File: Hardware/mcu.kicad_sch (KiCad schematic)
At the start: 20 parts, among them J2 Conn_01x03, SW2 SW_Push, SW3 SW_Push, U2 W25Q128JVS, U3 RP2040, Y1 ABM8-272-T3

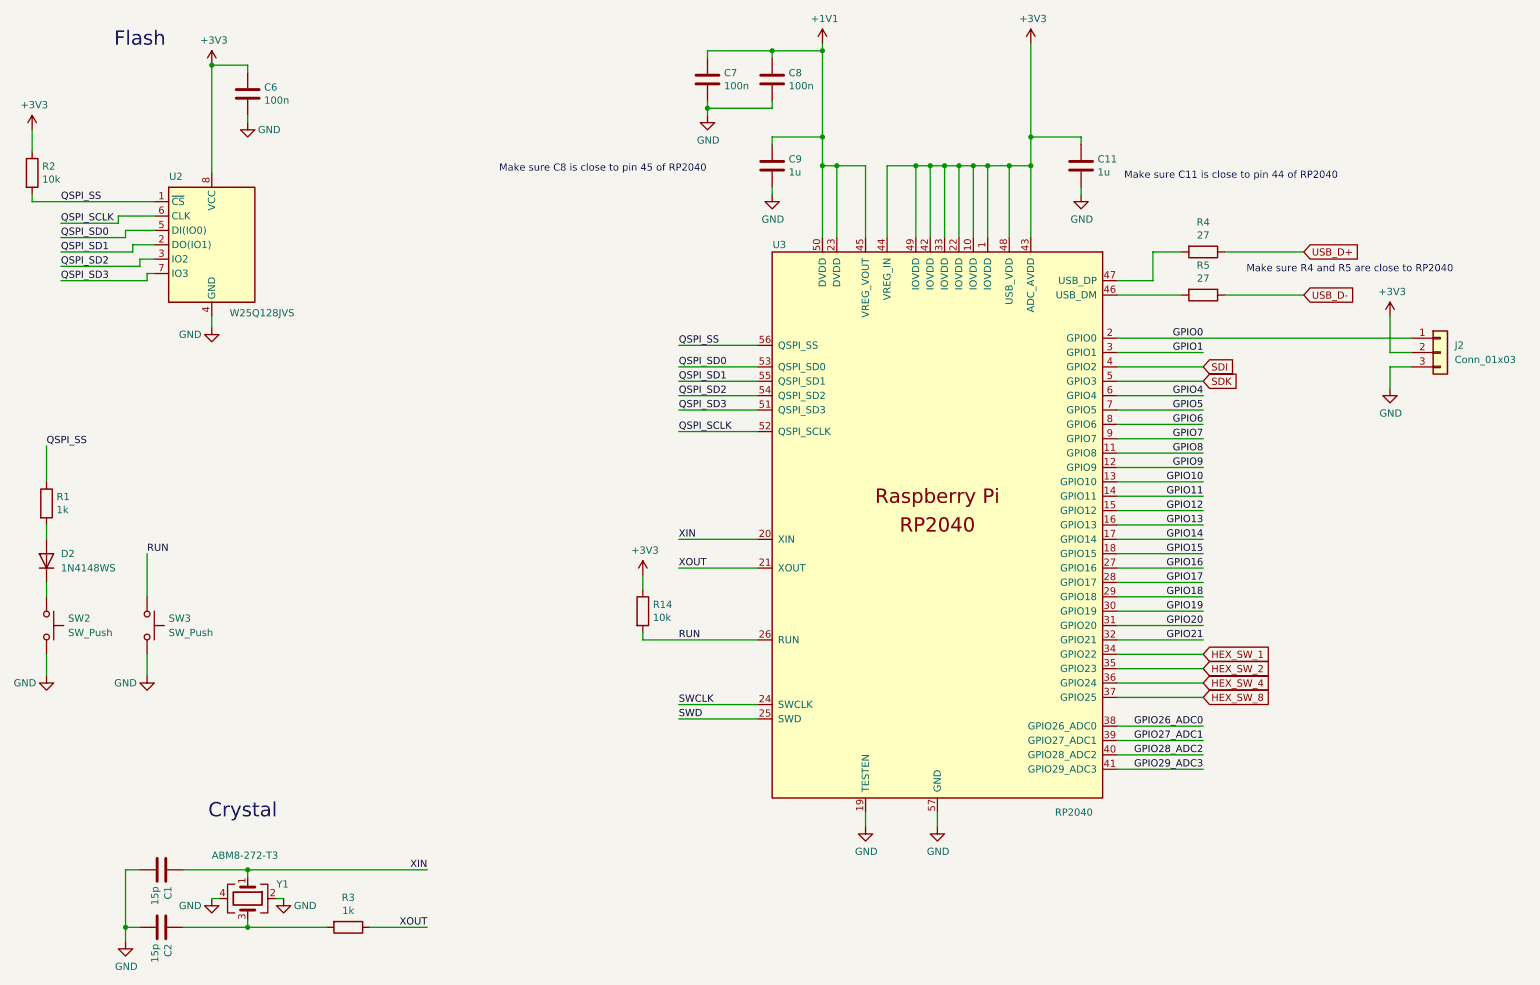
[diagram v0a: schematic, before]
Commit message: Added new components to sch and pcb and redid the routing and layout of pcb
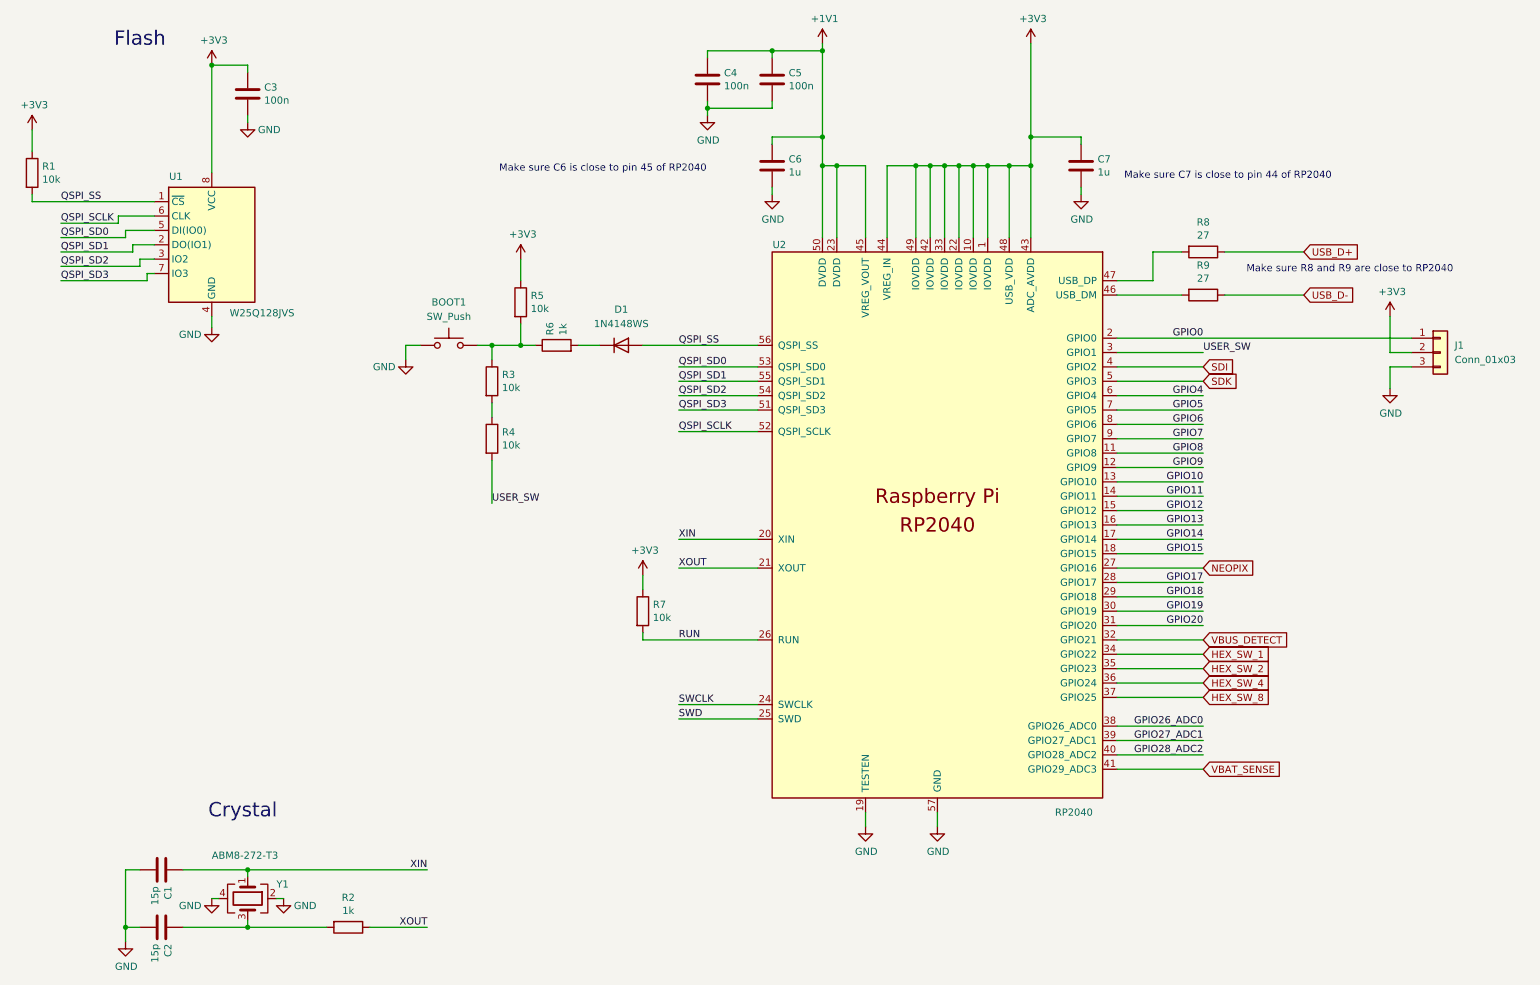
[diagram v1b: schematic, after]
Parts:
- removed SW3: SW_Push, duso:NanoT-AS, symbol Switch:SW_Push
- added R3, R4, R5: 10k, Resistor_SMD:R_0402_1005Metric, symbol Device:R
- renumbered SW2 to BOOT1, C6 to C3, C7 to C4, C8 to C5, C9 to C6, C11 to C7, D2 to D1, J2 to J1, R2 to R1, R3 to R2, R1 to R6, R14 to R7, R4 to R8, R5 to R9, U2 to U1, U3 to U2
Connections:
- net +3V3: now also R5.1
- net GND: now also BOOT1.1; no longer BOOT1.2
- net QSPI_SS: now also D1.2 (A); no longer R6.1
- net at D1.1 (K): now also R6.2; no longer BOOT1.1
- net GPIO1 renamed USER_SW
- net USER_SW: now also R4.2
- net GPIO16 renamed NEOPIX
- net GPIO21 renamed VBUS_DETECT
- net GPIO29_ADC3 renamed VBAT_SENSE
- new net: R3.2, R4.1
- new net: BOOT1.2, R3.1, R5.2, R6.1
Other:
- note added: "Make sure C6 is close to pin 45 of RP2040"
- note added: "Make sure C7 is close to pin 44 of RP2040"
- note added: "Make sure R8 and R9 are close to RP2040"
- note removed: "Make sure C11 is close to pin 44 of RP2040"
- note removed: "Make sure C8 is close to pin 45 of RP2040"
- note removed: "Make sure R4 and R5 are close to RP2040"
- moved on the sheet: BOOT1, D1, R6

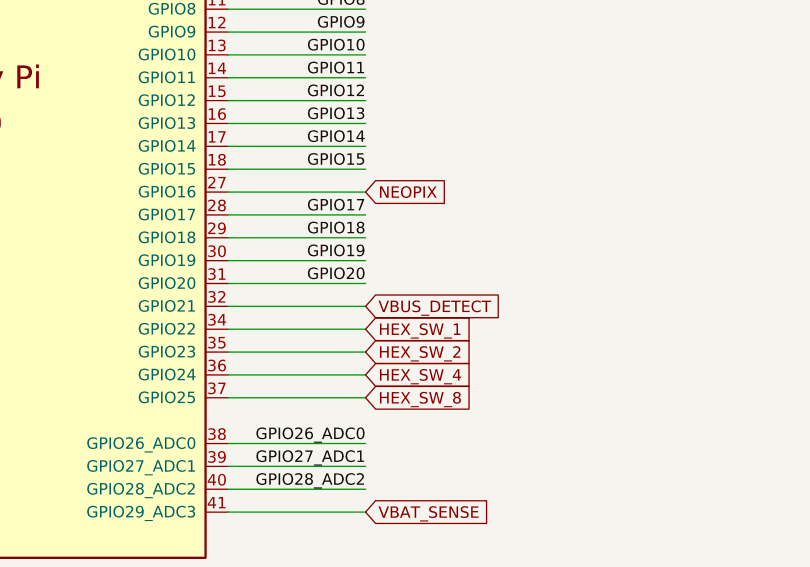
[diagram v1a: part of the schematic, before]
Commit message: Moved VBUS_DETECT from GPIO21 to GPIO19 to follow the rp2040 datasheet, updated some silkscreen
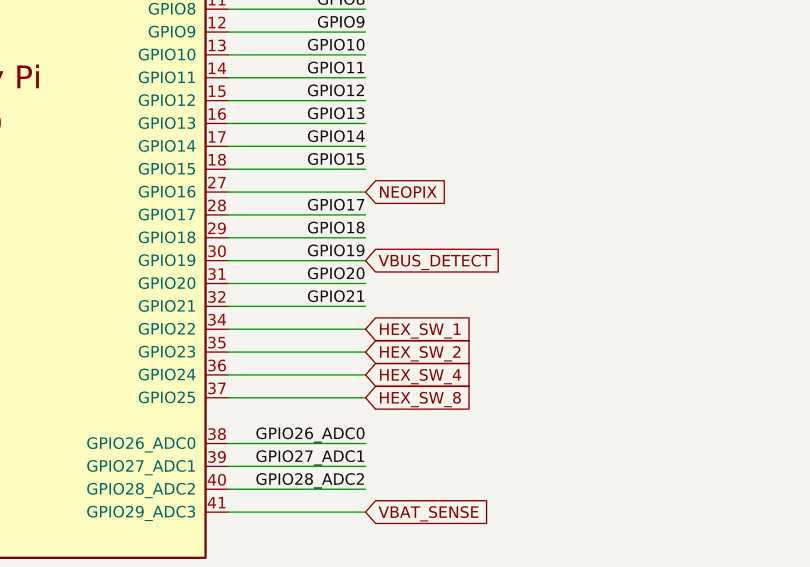
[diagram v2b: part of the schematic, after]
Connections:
- net GPIO19 is gone; now on net VBUS_DETECT: U2.30 (GPIO19)
- net VBUS_DETECT: no longer U2.32 (GPIO21)
- new net GPIO21: U2.32 (GPIO21)
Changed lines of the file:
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@@
+	(wire
+		(pts
+			(xy 212.09 124.46) (xy 227.33 124.46)
+		)
+		(stroke
+			(width 0)
+			(type default)
+		)
+	)
 	(wire
 		(pts
@@
 		(pts
 			(xy 39.37 57.15) (xy 39.37 58.42)
-		)
-		(stroke
-			(width 0)
-			(type default)
-		)
-	)
-	(wire
-		(pts
-			(xy 212.09 124.46) (xy 227.33 124.46)
 		)
 		(stroke
@@
 			)
 			(justify left bottom)
+		)
+	)
+	(label "GPIO21"
+		(at 227.33 124.46 180)
+		(fields_autoplaced yes)
+		(effects
+			(font
+				(size 1.27 1.27)
+			)
+			(justify right bottom)
 		)
 	)
@@
 	(global_label "VBUS_DETECT"
 		(shape input)
-		(at 227.33 124.46 0)
+		(at 227.33 119.38 0)
 		(fields_autoplaced yes)
 		(effects
@@
 		)
 		(property "Intersheetrefs" "${INTERSHEET_REFS}"
-			(at 242.9546 124.46 0)
+			(at 242.9546 119.38 0)
 			(effects
 				(font

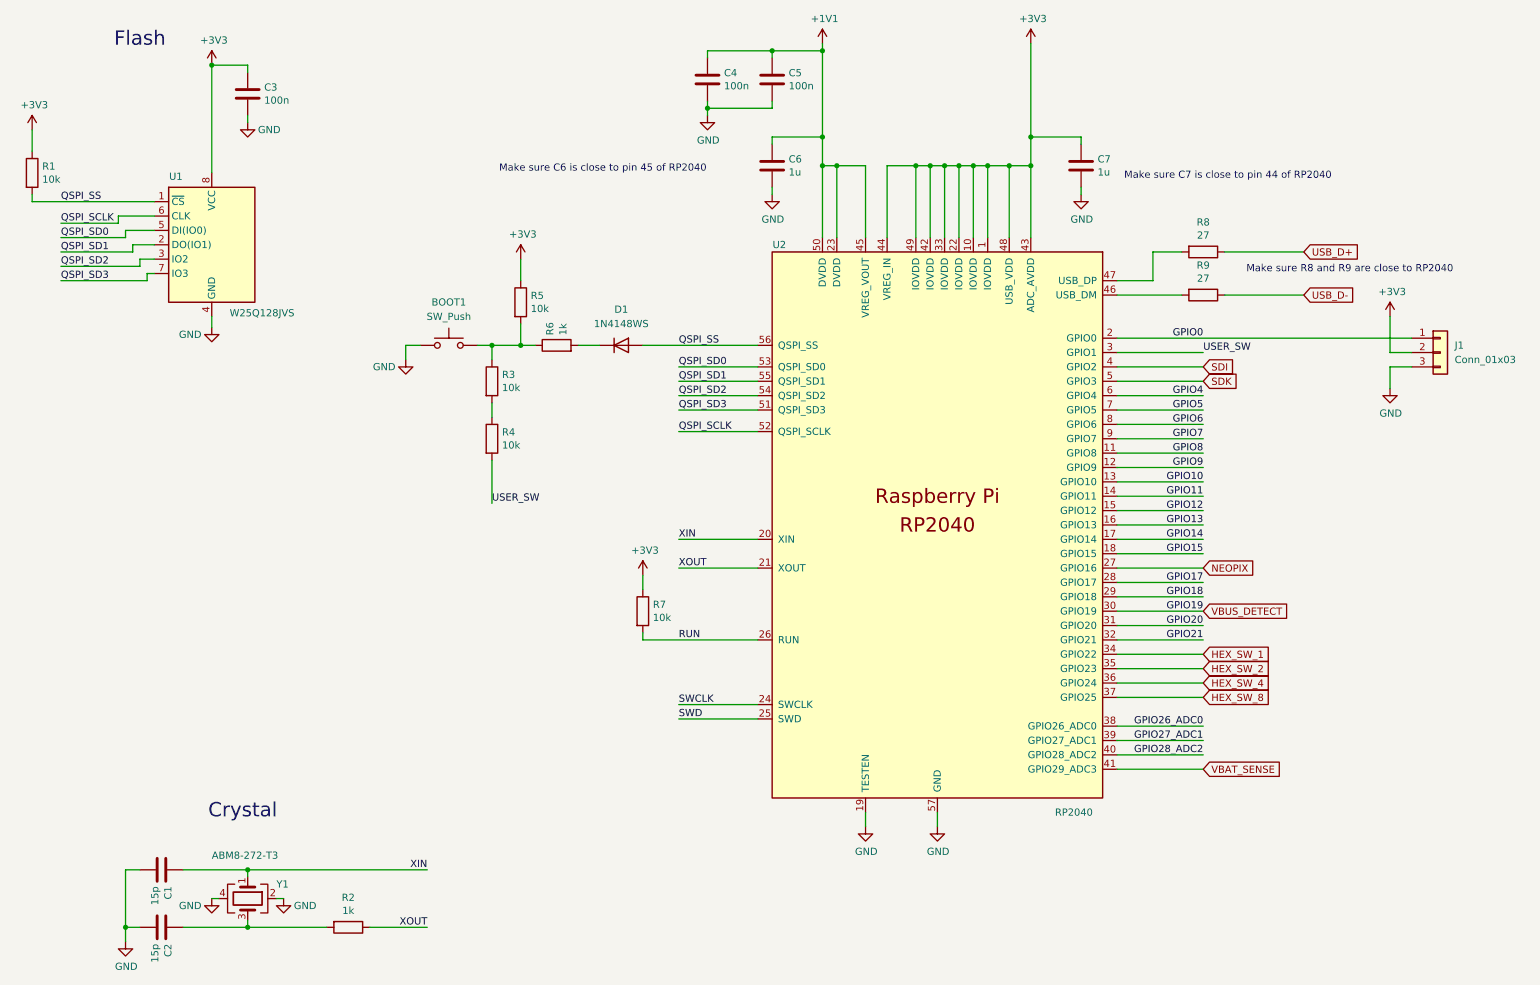
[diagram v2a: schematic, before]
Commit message: Added external batt switch pin and bypass 0ohm res, changed ldo for smaller 600mA
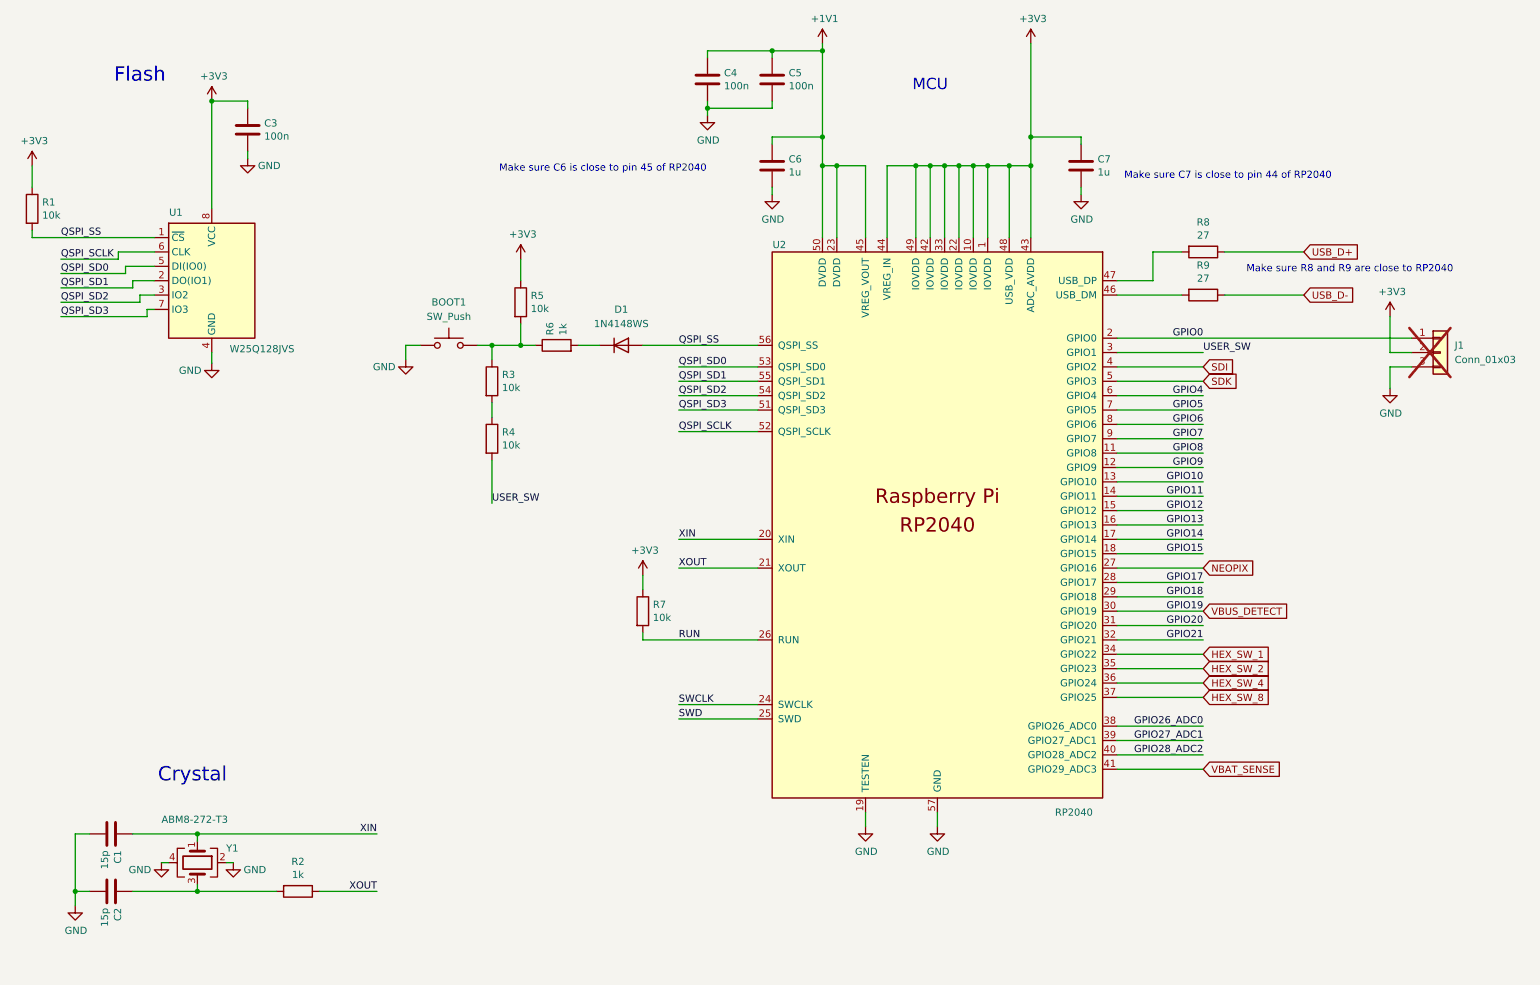
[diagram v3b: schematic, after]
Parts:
- J1: now not fitted
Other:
- note added: "MCU"
- moved on the sheet: C1, C2, C3, R1, R2, U1, Y1

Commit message: Board review fixes
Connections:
- net GPIO11 renamed SDO
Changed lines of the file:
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@@
+		)
+	)
+	(label "GPIO14"
+		(at 227.33 106.68 180)
+		(fields_autoplaced yes)
+		(effects
+			(font
+				(size 1.27 1.27)
+			)
+			(justify right bottom)
 		)
 	)
@@
 		)
 	)
-	(label "GPIO14"
-		(at 227.33 106.68 180)
-		(fields_autoplaced yes)
-		(effects
-			(font
-				(size 1.27 1.27)
-			)
-			(justify right bottom)
-		)
-	)
 	(label "QSPI_SS"
 		(at 134.62 72.39 0)
@@
 		)
 	)
-	(label "GPIO11"
-		(at 227.33 99.06 180)
-		(fields_autoplaced yes)
-		(effects
-			(font
-				(size 1.27 1.27)
-			)
-			(justify right bottom)
-		)
-	)
 	(label "QSPI_SCLK"
 		(at 134.62 87.63 0)
@@
 			(effects
 				(font
+					(size 1.27 1.27)
+				)
+				(justify left)
+				(hide yes)
+			)
+		)
+	)
+	(global_label "SDO"
+		(shape input)
+		(at 227.33 99.06 0)
+		(fields_autoplaced yes)
+		(effects
+			(font
+				(size 1.27 1.27)
+			)
+			(justify left)
+		)
+		(property "Intersheetrefs" "${INTERSHEET_REFS}"
+			(at 234.1252 99.06 0)
+			(effects
+				(font
